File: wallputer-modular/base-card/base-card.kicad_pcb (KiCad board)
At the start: 2 copper layers, 99.7 x 99.7 mm, 1 part

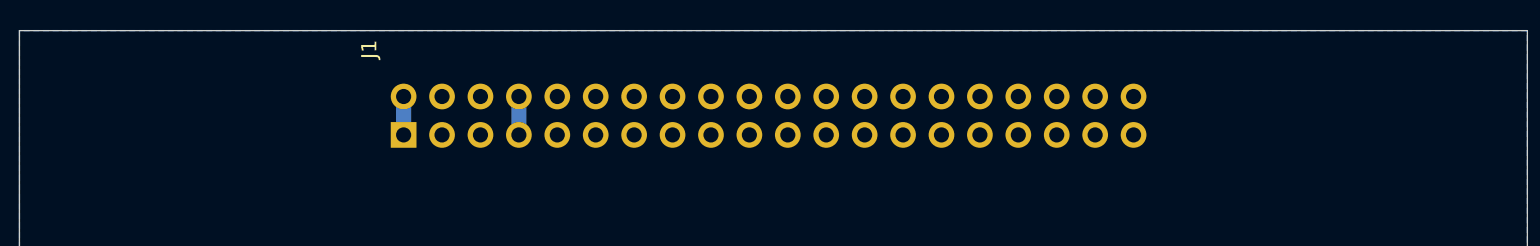
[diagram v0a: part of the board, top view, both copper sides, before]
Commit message: add card name
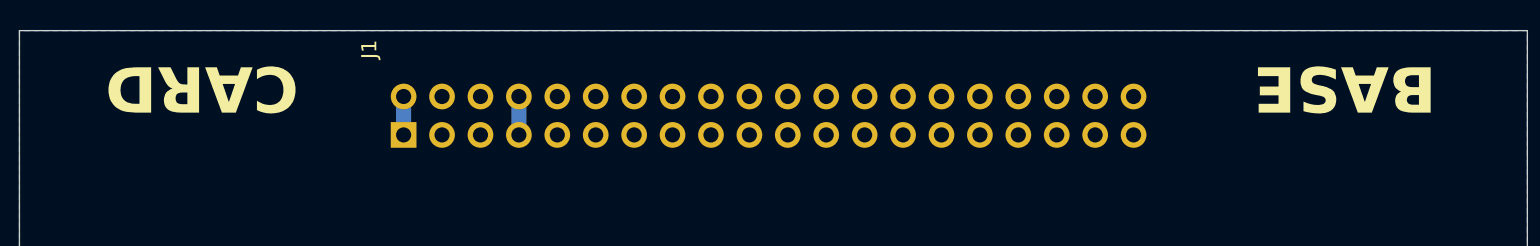
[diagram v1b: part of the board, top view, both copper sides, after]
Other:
- board text added: "BASE"
- board text added: "CARD"
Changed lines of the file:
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@@
 		(layer "Edge.Cuts")
+	)
+	(gr_text "BASE"
+		(at 151.13 67.31 180)
+		(layer "F.SilkS")
+		(effects
+			(font
+				(size 3 3)
+				(thickness 0.5)
+				(bold yes)
+			)
+		)
+	)
+	(gr_text "CARD\n"
+		(at 75.565 67.31 180)
+		(layer "F.SilkS")
+		(effects
+			(font
+				(size 3 3)
+				(thickness 0.5)
+				(bold yes)
+			)
+		)
 	)
 	(segment
